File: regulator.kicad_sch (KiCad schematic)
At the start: 10 parts, among them U3 LT8607

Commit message: Switching converter for 12 V -> 5V. LDO for 5->3
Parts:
- added U4: TLV73333PDBV, Package_TO_SOT_SMD:SOT-23-5, symbol Regulator_Linear:TLV73333PDBV
- R2: value 59.0k -> 102k
- R3: value 18.2k -> 18.7k
- U3: value LT8607 -> LT8608EMSE; symbol motion-sensor-syms:IC_LT8607_ANALOG -> motion-sensor-syms:IC_LT860xxMSE_ANALOG
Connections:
- net GND: now also U4.2 (GND)
- net V_{IN} renamed VIN
- net V_{OUT}: no longer names the net of C3.1, L1.2, R2.1
- net V_{OUT}: now also U4.1 (IN), U4.3 (EN)
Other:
- note added: "V_{OUT} is 5 V V_{REF} is 778 mV"
- note removed: "V_{OUT} is 3.3 V. V_{REF} is 778 mV"
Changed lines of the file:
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@@
 		)
 	)
-	(text "V_{OUT} is 3.3 V. V_{REF} is 778 mV"
-		(exclude_from_sim no)
-		(at 161.29 60.96 0)
+	(text "V_{OUT} is 5 V\nV_{REF} is 778 mV"
+		(exclude_from_sim no)
+		(at 139.7 43.18 0)
 		(effects
 			(font
@@
 	)
 	(junction
+		(at 160.02 78.74)
+		(diameter 0)
+		(color 0 0 0 0)
+	)
+	(junction
 		(at 148.59 78.74)
 		(diameter 0)
@@
 	)
 	(junction
+		(at 179.07 78.74)
+		(diameter 0)
+		(color 0 0 0 0)
+	)
+	(junction
 		(at 71.12 71.12)
 		(diameter 0)
@@
 		(color 0 0 0 0)
 	)
-	(junction
-		(at 160.02 78.74)
-		(diameter 0)
-		(color 0 0 0 0)
-	)
 	(no_connect
 		(at 124.46 83.82)
@@
 	(wire
 		(pts
+			(xy 179.07 78.74) (xy 179.07 81.28)
+		)
+		(stroke
+			(width 0)
+			(type default)
+		)
+	)
+	(wire
+		(pts
 			(xy 71.12 71.12) (xy 100.33 71.12)
 		)
@@
 	(wire
 		(pts
-			(xy 160.02 78.74) (xy 166.37 78.74)
-		)
-		(stroke
-			(width 0)
-			(type default)
-		)
-	)
-	(wire
-		(pts
 			(xy 104.14 88.9) (xy 87.63 88.9)
 		)
@@
 		)
 	)
-	(hierarchical_label "V_{OUT}"
-		(shape input)
-		(at 166.37 78.74 0)
-		(effects
-			(font
-				(size 1.27 1.27)
-			)
-			(justify left)
-		)
-	)
-	(hierarchical_label "V_{IN}"
+	(wire
+		(pts
+			(xy 160.02 78.74) (xy 179.07 78.74)
+		)
+		(stroke
+			(width 0)
+			(type default)
+		)
+	)
+	(hierarchical_label "VIN"
 		(shape input)
 		(at 64.77 71.12 180)
@@
 			)
 		)
-		(property "Value" "18.2k"
+		(property "Value" "18.7k"
 			(at 151.13 95.2499 0)
 			(effects
@@
 	)
 	(symbol
+		(lib_id "Regulator_Linear:TLV73333PDBV")
+		(at 186.69 81.28 0)
+		(unit 1)
+		(exclude_from_sim no)
+		(in_bom yes)
+		(on_board yes)
+		(dnp no)
+		(fields_autoplaced yes)
+		(property "Reference" "U4"
+			(at 186.69 72.39 0)
+			(effects
+				(font
+					(size 1.27 1.27)
+				)
+			)
+		)
+		(property "Value" "TLV73333PDBV"
+			(at 186.69 74.93 0)
+			(effects
+				(font
+					(size 1.27 1.27)
+				)
+			)
+		)
+		(property "Footprint" "Package_TO_SOT_SMD:SOT-23-5"
+			(at 186.69 73.025 0)
+			(effects
+				(font
+					(size 1.27 1.27)
+					(italic yes)
+				)
+				(hide yes)
+			)
+		)
+		(property "Datasheet" "http://www.ti.com/lit/ds/symlink/tlv733p.pdf"
+			(at 186.69 81.28 0)
+			(effects
+				(font
+					(size 1.27 1.27)
+				)
+				(hide yes)
+			)
+		)
+		(property "Description" "300mA Capacitor-Free Low Dropout Voltage Regulator, Fixed Output 3.3V, SOT-23-5"
+			(at 186.69 81.28 0)
+			(effects
+				(font
+					(size 1.27 1.27)
+				)
+				(hide yes)
+			)
+		)
+		(pin "4"
+		)
+		(pin "1"
+		)
+		(pin "5"
+		)
+		(pin "3"
+		)
+		(pin "2"
+		)
+		(instances
+			(project ""
+				(path "/d999e802-7382-49ed-b28b-80393e8497d9/20280cc7-411e-41b1-8687-9a48928895ed"
+					(reference "U4")
+					(unit 1)
+				)
+			)
+		)
+	)
+	(symbol
 		(lib_id "Device:C")
 		(at 130.81 74.93 0)
@@
 	)
 	(symbol
-		(lib_id "motion-sensor-syms:IC_LT8607_ANALOG")
+		(lib_id "motion-sensor-syms:IC_LT860xxMSE_ANALOG")
 		(at 114.3 81.28 0)
 		(unit 1)
@@
 			)
 		)
-		(property "Value" "LT8607"
+		(property "Value" "LT8608EMSE"
 			(at 114.3 66.04 0)
 			(effects
@@
 	(symbol
 		(lib_id "power:GND")
+		(at 186.69 88.9 0)
+		(unit 1)
+		(exclude_from_sim no)
+		(in_bom yes)
+		(on_board yes)
+		(dnp no)
+		(fields_autoplaced yes)
+		(property "Reference" "#PWR033"
+			(at 186.69 95.25 0)
+			(effects
+				(font
+					(size 1.27 1.27)
+				)
+				(hide yes)
+			)
+		)
+		(property "Value" "GND"
+			(at 186.69 93.98 0)
+			(effects
+				(font
+					(size 1.27 1.27)
+				)
+			)
+		)
+		(property "Footprint" ""
+			(at 186.69 88.9 0)
+			(effects
+				(font
+					(size 1.27 1.27)
+				)
+				(hide yes)
+			)
+		)
+		(property "Datasheet" ""
+			(at 186.69 88.9 0)
+			(effects
+				(font
+					(size 1.27 1.27)
+				)
+				(hide yes)
+			)
+		)
+		(property "Description" "Power symbol creates a global label with name \"GND\" , ground"
+			(at 186.69 88.9 0)
+			(effects
+				(font
+					(size 1.27 1.27)
+				)
+				(hide yes)
+			)
+		)
+		(pin "1"
+		)
+		(instances
+			(project "motion-sensor-hardware"
+				(path "/d999e802-7382-49ed-b28b-80393e8497d9/20280cc7-411e-41b1-8687-9a48928895ed"
+					(reference "#PWR033")
+					(unit 1)
+				)
+			)
+		)
+	)
+	(symbol
+		(lib_id "power:GND")
 		(at 99.06 104.14 0)
 		(unit 1)
@@
 			)
 		)
-		(property "Value" "59.0k"
+		(property "Value" "102k"
 			(at 151.13 85.0899 0)
 			(effects

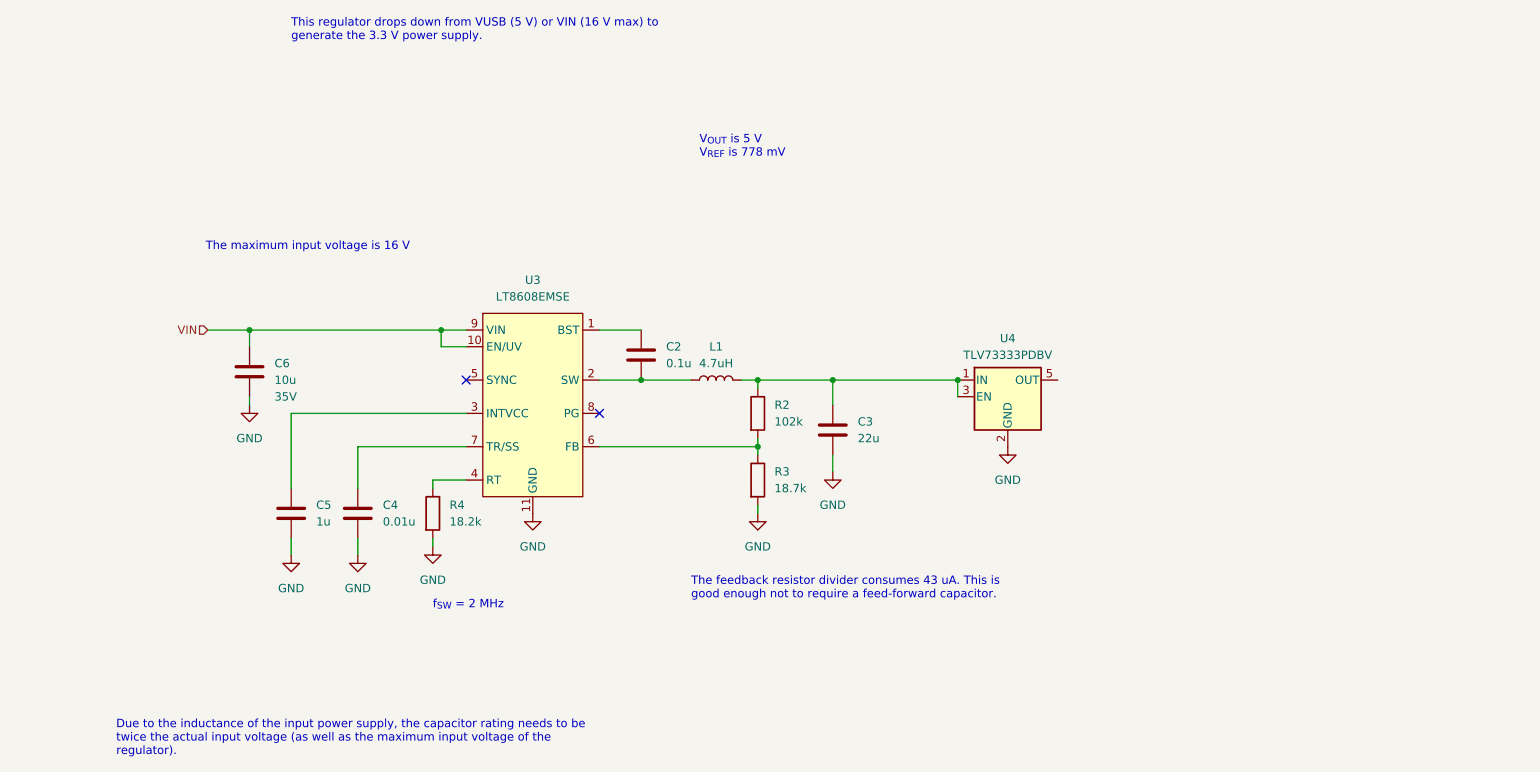
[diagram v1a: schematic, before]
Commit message: Added car charger circuits
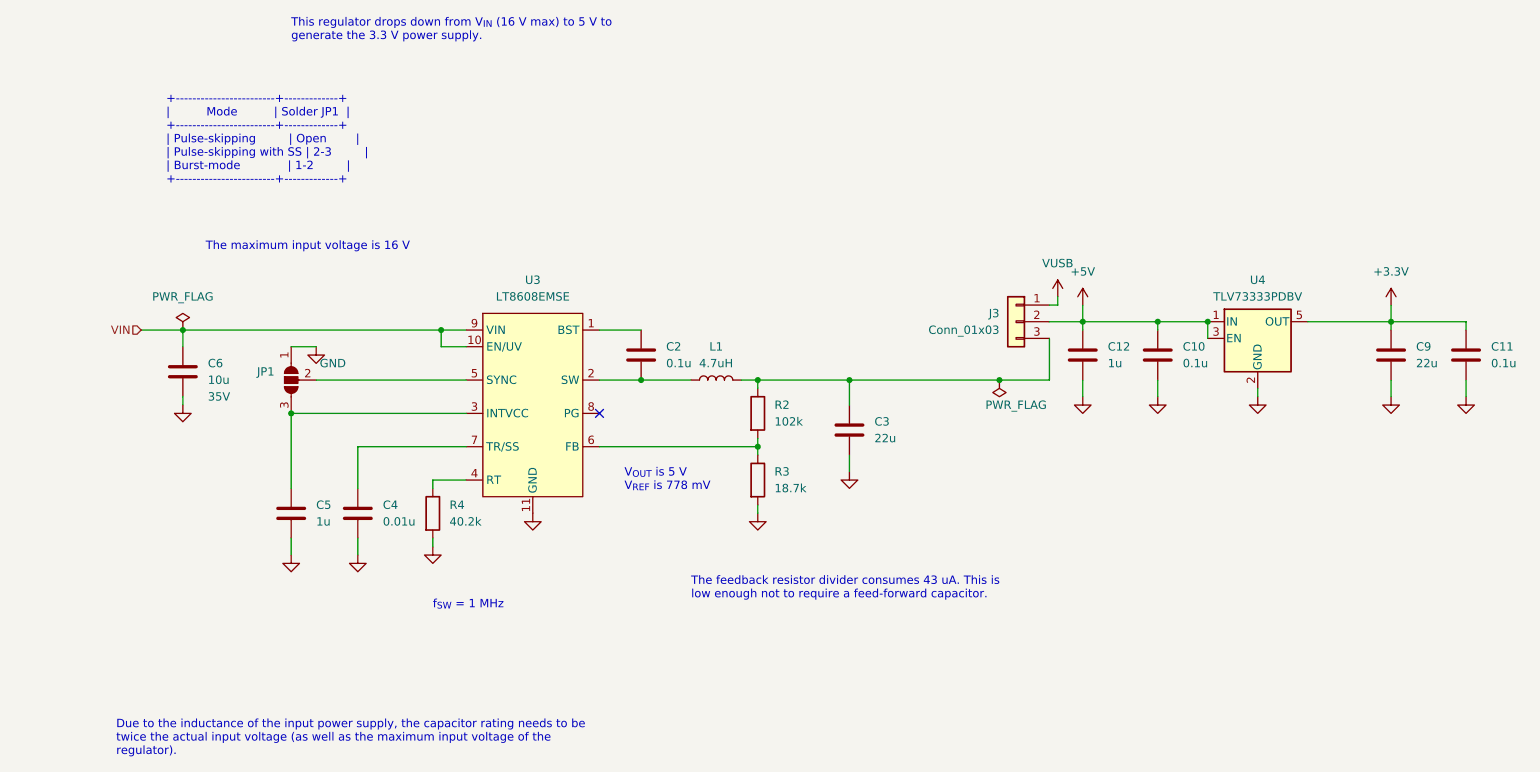
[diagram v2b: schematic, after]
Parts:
- added C10, C11: 0.1u, Capacitor_SMD:C_0805_2012Metric, symbol Device:C
- added C12: 1u, Capacitor_SMD:C_0805_2012Metric, symbol Device:C
- added C9: 22u, Capacitor_SMD:C_0805_2012Metric, symbol Device:C
- added J3: Conn_01x03, Connector_PinHeader_2.54mm:PinHeader_1x03_P2.54mm_Vertical, symbol Connector_Generic:Conn_01x03
- added JP1: SolderJumper_3_Open, Jumper:SolderJumper-3_P1.3mm_Open_Pad1.0x1.5mm, symbol Jumper:SolderJumper_3_Open
- C2: footprint (none) -> Capacitor_SMD:C_0805_2012Metric; JLCPCB (none) -> C106837
- C3: footprint (none) -> Capacitor_SMD:C_0805_2012Metric; JLCPCB (none) -> C5674
- C4: footprint (none) -> Capacitor_SMD:C_0805_2012Metric; JLCPCB (none) -> C85973
- C5, R2: footprint (none) -> Capacitor_SMD:C_0805_2012Metric; JLCPCB (none) -> C2999517
- C6: footprint (none) -> Capacitor_SMD:C_0805_2012Metric; JLCPCB (none) -> C6119888
- L1: footprint (none) -> Inductors:IND_54x52; JLCPCB (none) -> C41413058
- R3: footprint (none) -> Capacitor_SMD:C_0805_2012Metric; JLCPCB (none) -> C2933348
- R4: value 18.2k -> 40.2k; footprint (none) -> Capacitor_SMD:C_0805_2012Metric; JLCPCB (none) -> C17678
- U3: footprint (none) -> Package_SO:MSOP-10-1EP_3x3mm_P0.5mm_EP1.68x1.88mm; JLCPCB (none) -> C462620
- U4: JLCPCB (none) -> C134139
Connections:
- net GND: now also C10.2, C11.2, C12.2, C9.2, JP1.1 (A)
- net at C3.1, L1.2, R2.1: now also J3.3 (Pin_3); no longer U4.1 (IN), U4.3 (EN)
- net +3.3V: now reaches U4.5 (OUT)
- net +3.3V: now also C11.1, C9.1
- net at C5.1, U3.3 (INTVCC): now also JP1.3 (B)
- net at U3.5 (SYNC): now also JP1.2 (C)
- new net +5V: C10.1, C12.1, J3.2 (Pin_2), U4.1 (IN), U4.3 (EN)
- new net VUSB: J3.1 (Pin_1)
- no-connect marks 2 -> 1
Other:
- note added: "+------------------------+-------------+ | Mode | Solder JP1 | +------------------------+-------------+ | Pulse-skipping | Open | | Pulse-skipping with SS | 2-3 | | Burst-mode | 1-2 | +------------------------+-------------+"
- note added: "The feedback resistor divider consumes 43 uA. This is low enough not to require a feed-forward capacitor."
- note added: "This regulator drops down from V_{IN} (16 V max) to 5 V to generate the 3.3 V power supply."
- note added: "f_{SW} = 1 MHz"
- note removed: "The feedback resistor divider consumes 43 uA. This is good enough not to require a feed-forward capacitor."
- note removed: "This regulator drops down from VUSB (5 V) or VIN (16 V max) to generate the 3.3 V power supply."
- note removed: "f_{SW} = 2 MHz"
- moved on the sheet: C3, C6, U4

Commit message: Added decoupling cap for LED and bigger cap for module
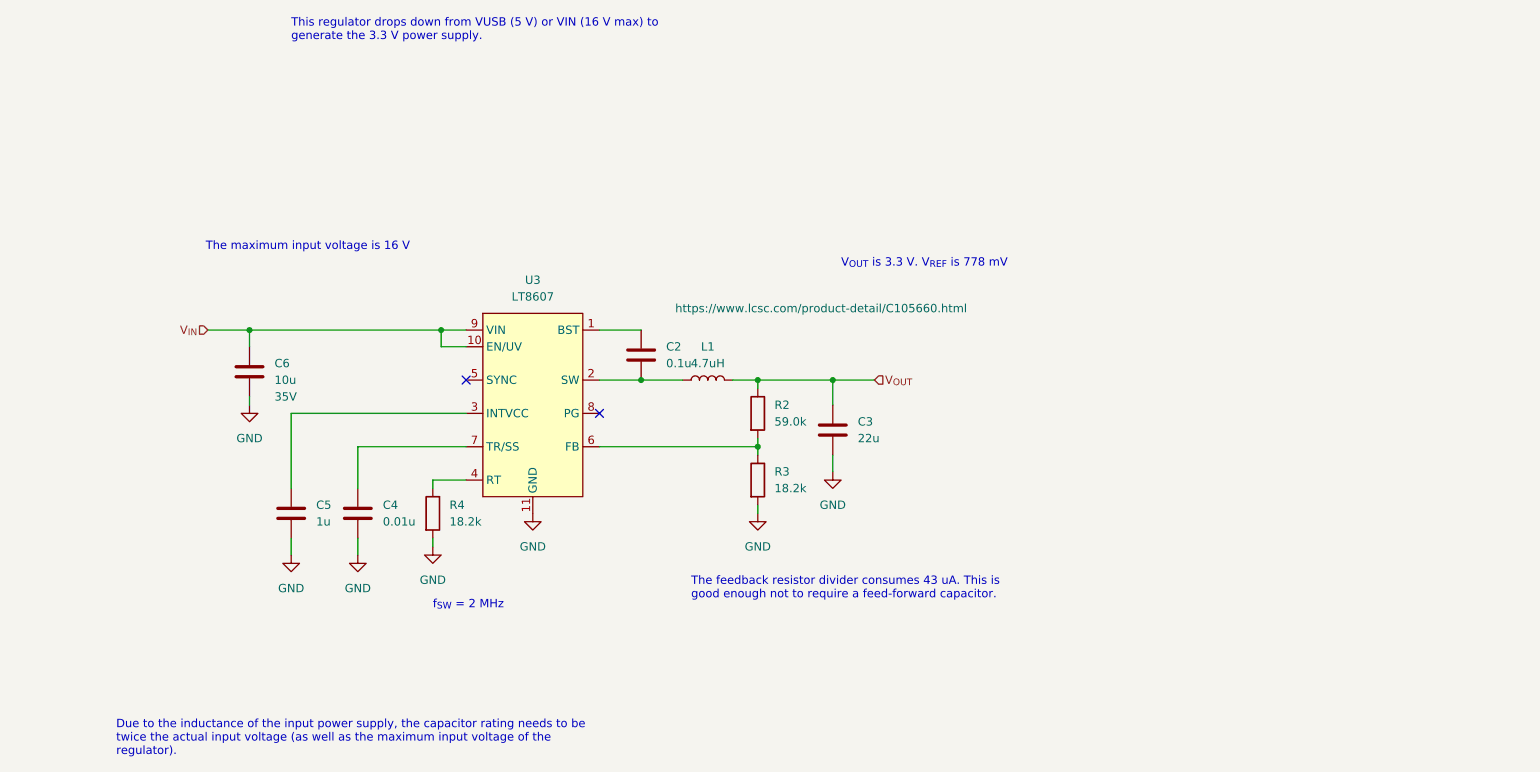
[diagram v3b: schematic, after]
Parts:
- removed C10, C11: 0.1u, Capacitor_SMD:C_0805_2012Metric, symbol Device:C
- removed C12: 1u, Capacitor_SMD:C_0805_2012Metric, symbol Device:C
- removed C9: 22u, Capacitor_SMD:C_0805_2012Metric, symbol Device:C
- removed J3: Conn_01x03, Connector_PinHeader_2.54mm:PinHeader_1x03_P2.54mm_Vertical, symbol Connector_Generic:Conn_01x03
- removed JP1: SolderJumper_3_Open, Jumper:SolderJumper-3_P1.3mm_Open_Pad1.0x1.5mm, symbol Jumper:SolderJumper_3_Open
- removed U4: TLV73333PDBV, Package_TO_SOT_SMD:SOT-23-5, symbol Regulator_Linear:TLV73333PDBV
- C2: footprint Capacitor_SMD:C_0805_2012Metric -> (none); JLCPCB C106837 -> (none)
- C3: footprint Capacitor_SMD:C_0805_2012Metric -> (none); JLCPCB C5674 -> (none)
- C4: footprint Capacitor_SMD:C_0805_2012Metric -> (none); JLCPCB C85973 -> (none)
- C5: footprint Capacitor_SMD:C_0805_2012Metric -> (none); JLCPCB C2999517 -> (none)
- C6: footprint Capacitor_SMD:C_0805_2012Metric -> (none); JLCPCB C6119888 -> (none)
- L1: footprint Inductors:IND_54x52 -> (none); JLCPCB C41413058 -> (none); JLCPCBLink (none) -> https://www.lcsc.com/product-detail/C105660.html
- R2: value 102k -> 59.0k; footprint Capacitor_SMD:C_0805_2012Metric -> (none); JLCPCB C2999517 -> (none)
- R3: value 18.7k -> 18.2k; footprint Capacitor_SMD:C_0805_2012Metric -> (none); JLCPCB C2933348 -> (none)
- R4: value 40.2k -> 18.2k; footprint Capacitor_SMD:C_0805_2012Metric -> (none); JLCPCB C17678 -> (none)
- U3: value LT8608EMSE -> LT8607; footprint Package_SO:MSOP-10-1EP_3x3mm_P0.5mm_EP1.68x1.88mm -> (none); symbol motion-sensor-syms:IC_LT860xxMSE_ANALOG -> motion-sensor-syms:IC_LT8607_ANALOG; JLCPCB C462620 -> (none)
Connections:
- net V_{OUT}: now reaches C3.1, L1.2, R2.1
- net VIN renamed V_{IN}
- no-connect marks 1 -> 2
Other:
- note added: "The feedback resistor divider consumes 43 uA. This is good enough not to require a feed-forward capacitor."
- note added: "This regulator drops down from VUSB (5 V) or VIN (16 V max) to generate the 3.3 V power supply."
- note added: "V_{OUT} is 3.3 V. V_{REF} is 778 mV"
- note added: "f_{SW} = 2 MHz"
- note removed: "+------------------------+-------------+ | Mode | Solder JP1 | +------------------------+-------------+ | Pulse-skipping | Open | | Pulse-skipping with SS | 2-3 | | Burst-mode | 1-2 | +------------------------+-------------+"
- note removed: "The feedback resistor divider consumes 43 uA. This is low enough not to require a feed-forward capacitor."
- note removed: "This regulator drops down from V_{IN} (16 V max) to 5 V to generate the 3.3 V power supply."
- note removed: "V_{OUT} is 5 V V_{REF} is 778 mV"
- note removed: "f_{SW} = 1 MHz"
- moved on the sheet: C3, C6, L1

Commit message: Schematic relatively complete
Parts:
- removed U3: LT8607, symbol motion-sensor-syms:IC_LT8607_ANALOG
- added C11, C13, C14: 0.1u, Capacitor_SMD:C_0805_2012Metric, symbol Device:C
- added C12, C17: 47u, Capacitor_SMD:C_0805_2012Metric, symbol Device:C
- added C15: 10u, Capacitor_SMD:C_0805_2012Metric, symbol Device:C
- added C16: 47u, Capacitor_SMD:C_1206_3216Metric, symbol Device:C
- added L2: 6.8uH, Inductor_SMD:L_Changjiang_FXL0630, symbol Device:L
- added R16: 10k, symbol Device:R
- added U3, U4: AP62200TWU-7, Package_TO_SOT_SMD:SOT-23-6, symbol motion-sensor-syms:ADP6220x
- C2: footprint (none) -> Capacitor_SMD:C_0805_2012Metric; JLCPCB (none) -> C106837
- C3: value 22u -> 47u; footprint (none) -> Capacitor_SMD:C_1206_3216Metric; JLCPCB (none) -> C96123; Voltage (none) -> 10V
- C4: value 0.01u -> 0.1u; footprint (none) -> Capacitor_SMD:C_0805_2012Metric; JLCPCB (none) -> C106837
- C5: value 1u -> 0.1u; footprint (none) -> Capacitor_SMD:C_0805_2012Metric; JLCPCB (none) -> C106837
- C6: footprint (none) -> Capacitor_SMD:C_0805_2012Metric; JLCPCB (none) -> C440198; Voltage 35V -> 50V
- L1: value 4.7uH -> 6.8uH; footprint (none) -> Inductor_SMD:L_Changjiang_FXL0630; JLCPCB (none) -> C167221; JLCPCBLink https://www.lcsc.com/product-detail/C105660.html -> (none); PN (none) -> FXL0630-6R8-M
- R2: value 59.0k -> 100k
- R3: value 18.2k -> 18k
- R4: value 18.2k -> 33k
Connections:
- net GND: now also C5.1, C11.1, C12.2, C13.1, C14.1, C15.2, C16.2, C17.2, R16.2, U3.1 (GND), U4.1 (GND); no longer C4.2, C5.2, R4.2
- net V_{IN}: now also C5.2, C11.2, C15.1, U3.3 (VIN), U4.3 (VIN)
- net +3.3V: now reaches R4.1
- net +3.3V: now also C12.1, C17.1, L2.2
- net at L1.1: now also C2.1, U3.2 (SW); no longer C2.2
- net at C4.1: now also L2.1, U4.2 (SW)
- net at R2.2, R3.1: now also U3.4 (FB)
- net V_{OUT} renamed +5V
- net +5V: now also C16.1
- new net: C4.2, U4.6 (BST)
- new net: C13.2, U3.5 (EN)
- new net: R16.1, R4.2, U4.4 (FB)
- new net: C2.2, U3.6 (BST)
- new net: C14.2, U4.5 (EN)
- no-connect marks 2 -> 0
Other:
- note added: "Cd(nf) ≈ 0.278×td(ms)"
- note added: "V_{REF} is 763 mV"
- note added: "f_{SW} = 750 kHz"
- note removed: "Due to the inductance of the input power supply, the capacitor rating needs to be twice the actual input voltage (as well as the maximum input voltage of the regulator)."
- note removed: "The feedback resistor divider consumes 43 uA. This is good enough not to require a feed-forward capacitor."
- note removed: "V_{OUT} is 3.3 V. V_{REF} is 778 mV"
- note removed: "f_{SW} = 2 MHz"
- moved on the sheet: C3, C6, L1, R2, R3
